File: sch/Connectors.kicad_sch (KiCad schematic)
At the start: 4 parts, among them J1 Conn_01x16_Pin, J2 Conn_01x12_Pin, J4 Conn_01x02_MountingPin, J5 Conn_01x04_MountingPin

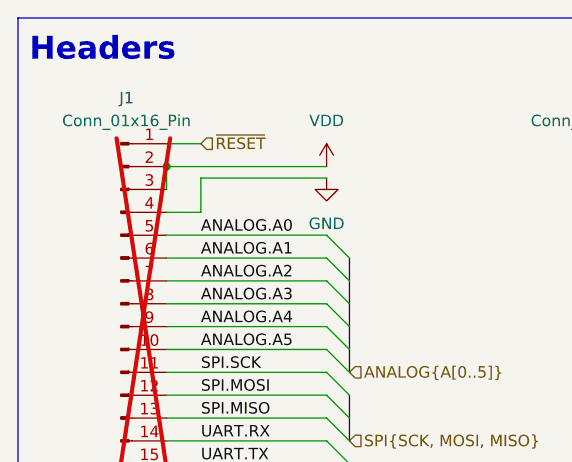
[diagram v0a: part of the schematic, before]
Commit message: Adjusted pinout, added pinout diagram
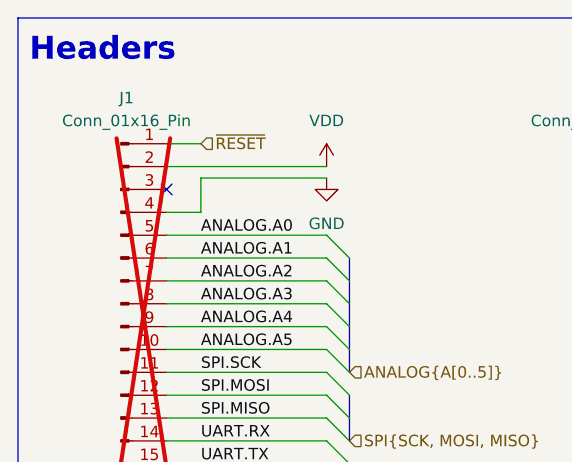
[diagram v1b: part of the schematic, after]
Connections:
- net VDD: no longer J1.3 (Pin_3)
- no-connect marks 0 -> 1
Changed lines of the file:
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@@
-	)
-	(junction
-		(at 68.58 91.44)
-		(diameter 0)
-		(color 0 0 0 0)
 	)
 	(junction
@@
 		(color 0 0 0 0)
 	)
+	(no_connect
+		(at 68.58 93.98)
+	)
 	(bus_entry
 		(at 144.78 116.84)
@@
 		)
 		(stroke
-			(width 0)
-			(type default)
-		)
-	)
-	(wire
-		(pts
-			(xy 68.58 91.44) (xy 68.58 93.98)
-		)
-		(stroke
